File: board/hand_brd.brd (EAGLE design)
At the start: 61.9 x 76.2 mm, 133 parts, among them IC1 FT230XS, Q1 BC847ALT1SMD, Q2 16MHz, Q3 16MHz, U2 ATXMEGA128D4-AU

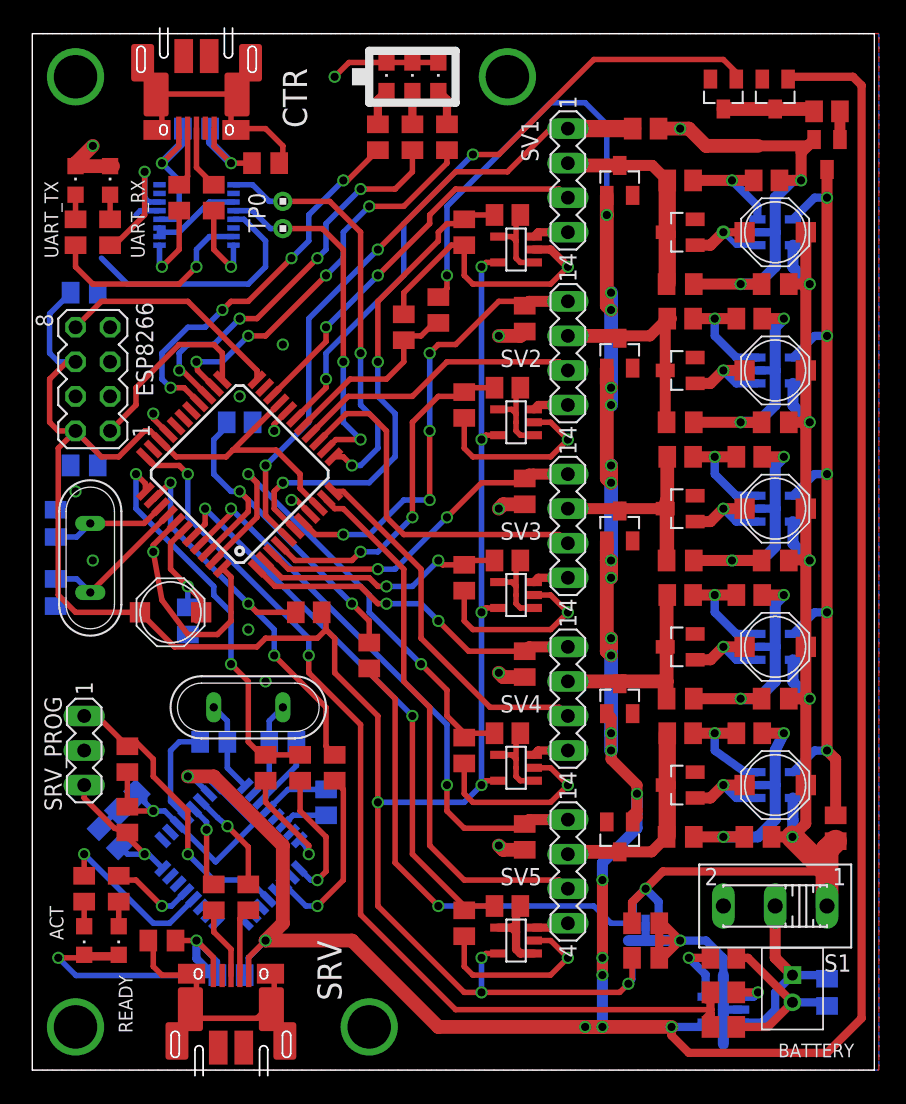
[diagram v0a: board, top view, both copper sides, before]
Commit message: Fix wrong USB model
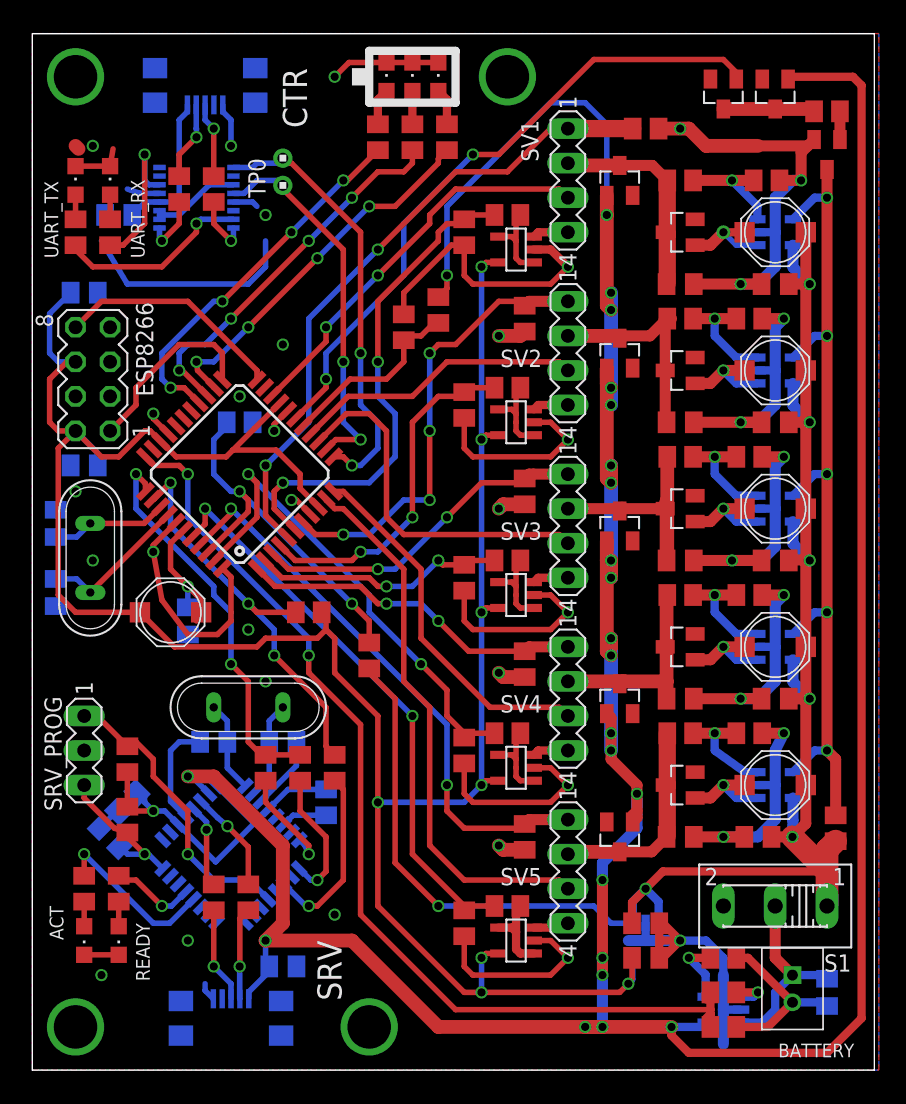
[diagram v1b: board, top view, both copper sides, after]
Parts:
- removed C13, C25: 100n, rcl:C0805K
- removed JP1, JP2: MICRO-USB-FCI-10103592, micro-usb-fci-10103592:MICRO-USB-FCI-10103592
- added U1, U3: (no value), MicroUSB:USB-MICRO-SMD
- moved C24 8.54 mm to (45.7, 62.2), turned to 0 degrees
- moved C12 3.86 mm to (57.8, 6.99), turned to 180 degrees
- moved TP_UART 3.18 mm to (57.8, 65.4)
- moved R27 2.62 mm to (50.2, 64.1)
- moved R28 2.62 mm to (52.7, 64.1)
- moved IC1 1.27 mm to (51.4, 63.5)
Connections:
- removed net N$11: JP1.3, R16.2
- removed net N$23: IC1.9, R28.1
- removed net USB2_D+: JP2.3, R27.2
- removed net USB2_D-: JP2.2, R28.2
- new net USBDM: IC1.9, R27.1
- new net USBDP: IC1.8, R28.1
- net GND: now also U1.GND1, U3.GND1; no longer C13.2, C25.2, JP1.5, JP2.5
- net N$10: now also U3.D-1; no longer JP1.2
- net N$18: now also R27.2, U1.D-1; no longer C25.1
- net N$22: now also R28.2, U1.D+1; no longer IC1.8, R27.1
- net N$8: now also R16.2, U3.D+1; no longer C13.1
- net V_USB2: now also U1.VBUS1; no longer JP2.1
- net V_USB_CHG: now also U3.VBUS1; no longer JP1.1
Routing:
- net GND: track 337.2 -> 303.8 mm, vias 40 -> 42
- net N$29: track 8.15 -> 0.00 mm
- net N$8: track 0.00 -> 7.04 mm, vias 0 -> 1
- net N$24: track 6.88 -> 0.00 mm
- net N$23: track 6.32 -> 0.00 mm, vias 1 -> 0
- net N$18: track 0.00 -> 5.77 mm, vias 0 -> 1
- net N$11: track 5.32 -> 0.00 mm
- net N$28: track 5.08 -> 0.00 mm
- net N$31: track 4.71 -> 0.00 mm
- net USB2_D+: track 4.69 -> 0.00 mm
- net USB2_D-: track 4.42 -> 0.00 mm
- net USBDP: track 0.00 -> 4.41 mm, vias 0 -> 1
- net USBDM: track 0.00 -> 4.41 mm, vias 0 -> 1
- net N$32: track 2.54 -> 0.00 mm
- net UART_RX: track 26.6 -> 28.4 mm
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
